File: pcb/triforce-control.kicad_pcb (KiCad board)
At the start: 2 copper layers, 75 x 86 mm, 17 parts, among them CON1 Conn_01x08, CON2 Conn_01x08, CON9 Conn_01x04, U1 ADAFRUIT_HUZZAH, U2 bno055, U3 LPC1768, U4 SN65HVD232

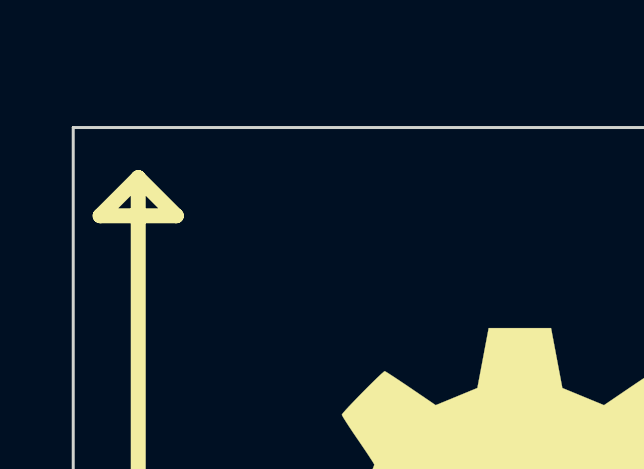
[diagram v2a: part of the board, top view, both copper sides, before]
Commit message: Started adding enclosure parts as footprints.
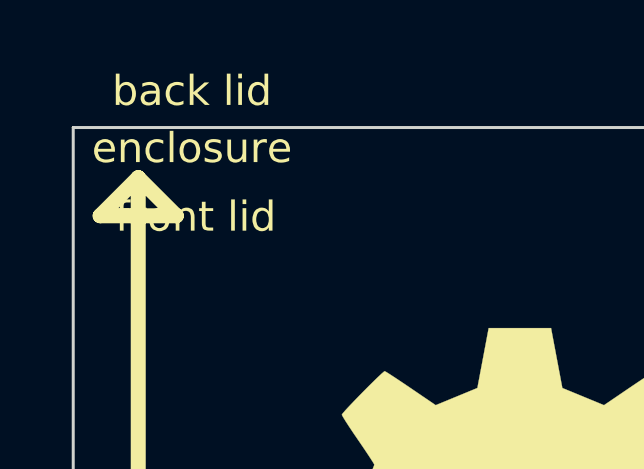
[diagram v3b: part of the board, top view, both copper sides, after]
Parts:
- added back lid: enclosure, Triforce_Fight_Controller:enclosure, F.Cu at (112.1, 51.3)
- added enclosure: enclosure, Triforce_Fight_Controller:enclosure, F.Cu at (112.1, 53.2)
- added enclosure: enclosure, Triforce_Fight_Controller:enclosure, F.Cu at (31.8, 36.7)
- added front lid: enclosure, Triforce_Fight_Controller:enclosure, F.Cu at (112.3, 55.5)
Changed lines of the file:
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@@
 (kicad_pcb (version 4) (host pcbnew 4.0.7-e2-6376~58~ubuntu16.04.1)
   (general
-    (links 52)
+    (links 0)
     (no_connects 0)
     (area 112.068999 53.108999 187.169001 139.209001)
@@
     (tracks 304)
     (zones 0)
-    (modules 17)
+    (modules 21)
     (nets 71)
   )
@@
     (add_net ESP_MBED_RX)
     (add_net ESP_MBED_TX)
+  )
+  (module Triforce_Fight_Controller:enclosure locked (layer F.Cu)
+    (at 112.268 55.499)
+    (attr virtual)
+    (fp_text reference "front lid" (at 3.937 0.635) (layer F.SilkS)
+      (effects (font (size 1 1) (thickness 0.15)))
+    )
+    (fp_text value enclosure (at 0 -0.5) (layer F.Fab)
+      (effects (font (size 1 1) (thickness 0.15)))
+    )
+    (model "TriforceFightController.3dshapes/J Bezel Closed.wrl"
+      (at (xyz 0.8149999999999999 -3.4 0.2))
+      (scale (xyz 1 1 1))
+      (rotate (xyz -90 0 0))
+    )
+  )
+  (module Triforce_Fight_Controller:enclosure locked (layer F.Cu)
+    (at 112.141 51.308)
+    (attr virtual)
+    (fp_text reference "back lid" (at 3.937 0.635) (layer F.SilkS)
+      (effects (font (size 1 1) (thickness 0.15)))
+    )
+    (fp_text value enclosure (at 0 -0.5) (layer F.Fab)
+      (effects (font (size 1 1) (thickness 0.15)))
+    )
+    (model "TriforceFightController.3dshapes/J Bezel Closed.wrl"
+      (at (xyz 0.8149999999999999 1.2 0.2))
+      (scale (xyz 1 1 1))
+      (rotate (xyz -270 0 0))
+    )
   )
   (module Symbols:KiCad-Logo2_6mm_SilkScreen (layer F.Cu)
@@
       (at (xyz 0 0 0))
       (scale (xyz 1 1 1))
+      (rotate (xyz 0 0 0))
+    )
+  )
+  (module Triforce_Fight_Controller:enclosure locked (layer F.Cu)
+    (at 112.141 53.213)
+    (attr virtual)
+    (fp_text reference enclosure (at 3.937 0.635) (layer F.SilkS)
+      (effects (font (size 1 1) (thickness 0.15)))
+    )
+    (fp_text value enclosure (at 0 -0.5) (layer F.Fab)
+      (effects (font (size 1 1) (thickness 0.15)))
+    )
+    (model "TriforceFightController.3dshapes/J Extrusion001.wrl"
+      (at (xyz 1.47 -3.4 0.71))
+      (scale (xyz 1 1 1))
+      (rotate (xyz 90 0 0))
+    )
+    (model "TriforceFightController.3dshapes/J Extrusion.wrl"
+      (at (xyz 1.47 -3.4 0.71))
+      (scale (xyz 1 1 1))
+      (rotate (xyz 90 0 0))
+    )
+  )
+  (module Triforce_Fight_Controller:enclosure (layer F.Cu)
+    (at 31.75 36.703)
+    (fp_text reference enclosure (at 0 1.27) (layer F.SilkS) hide
+      (effects (font (size 1 1) (thickness 0.15)))
+    )
+    (fp_text value enclosure (at 0 -0.5) (layer F.Fab)
+      (effects (font (size 1 1) (thickness 0.15)))
+    )
+    (model "TriforceFightController.3dshapes/J Extrusion001.wrl"
+      (at (xyz 0 0 0))
+      (scale (xyz 1 1 1))
+      (rotate (xyz 0 0 0))
+    )
+    (model "TriforceFightController.3dshapes/J Extrusion.wrl"
+      (at (xyz 0 0 0))
+      (scale (xyz 1 1 1))

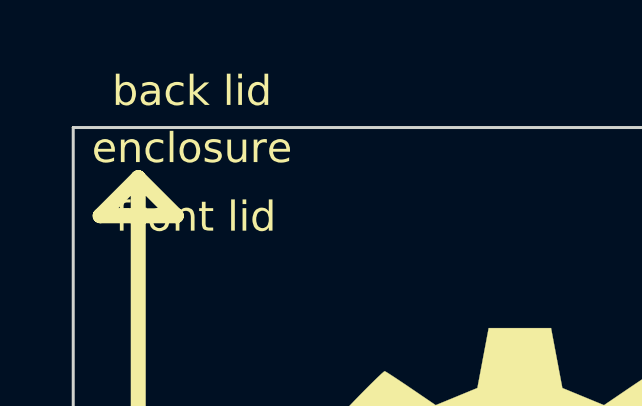
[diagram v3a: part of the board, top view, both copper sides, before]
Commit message: Added enclosure 3d shapes to PCB.
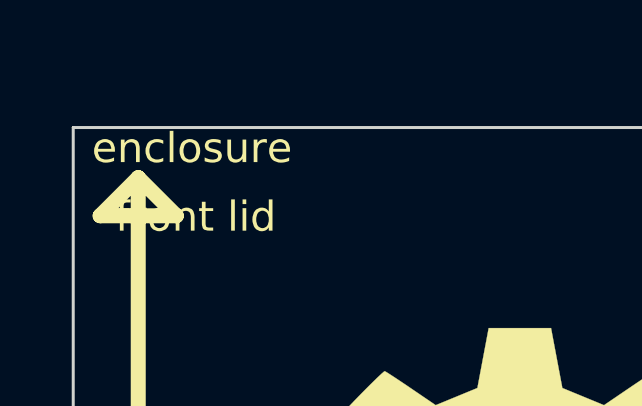
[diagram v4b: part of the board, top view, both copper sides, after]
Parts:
- removed the enclosure at (31.8, 36.7)
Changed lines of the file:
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@@
 (kicad_pcb (version 4) (host pcbnew 4.0.7-e2-6376~58~ubuntu16.04.1)
   (general
-    (links 0)
+    (links 52)
     (no_connects 0)
     (area 112.068999 53.108999 187.169001 139.209001)
@@
     (tracks 304)
     (zones 0)
-    (modules 21)
+    (modules 20)
     (nets 71)
   )
@@
     (at 112.141 51.308)
     (attr virtual)
-    (fp_text reference "back lid" (at 3.937 0.635) (layer F.SilkS)
+    (fp_text reference "back lid" (at 3.937 0.635) (layer F.SilkS) hide
       (effects (font (size 1 1) (thickness 0.15)))
     )
@@
     )
     (model "TriforceFightController.3dshapes/J Bezel Closed.wrl"
-      (at (xyz 0.8149999999999999 1.2 0.2))
+      (at (xyz 0.8149999999999999 1.2 0.3))
       (scale (xyz 1 1 1))
       (rotate (xyz -270 0 0))
@@
     )
   )
-  (module Triforce_Fight_Controller:enclosure (layer F.Cu)
-    (at 31.75 36.703)
-    (fp_text reference enclosure (at 0 1.27) (layer F.SilkS) hide
-      (effects (font (size 1 1) (thickness 0.15)))
-    )
-    (fp_text value enclosure (at 0 -0.5) (layer F.Fab)
-      (effects (font (size 1 1) (thickness 0.15)))
-    )
-    (model "TriforceFightController.3dshapes/J Extrusion001.wrl"
-      (at (xyz 0 0 0))
-      (scale (xyz 1 1 1))
-      (rotate (xyz 0 0 0))
-    )
-    (model "TriforceFightController.3dshapes/J Extrusion.wrl"
-      (at (xyz 0 0 0))
-      (scale (xyz 1 1 1))
-      (rotate (xyz 0 0 0))
-    )
-  )

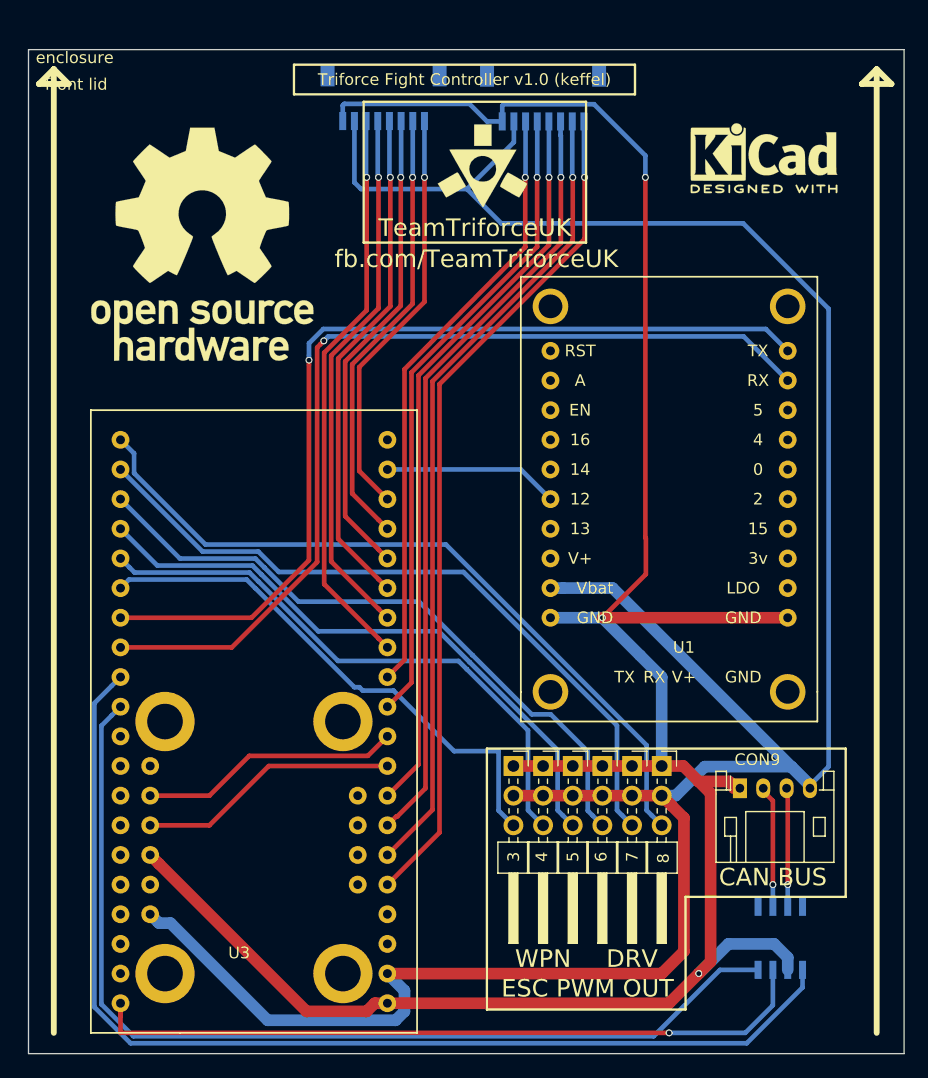
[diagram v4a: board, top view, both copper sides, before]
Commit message: Started v2.x work, integrating developement boards into PCB.
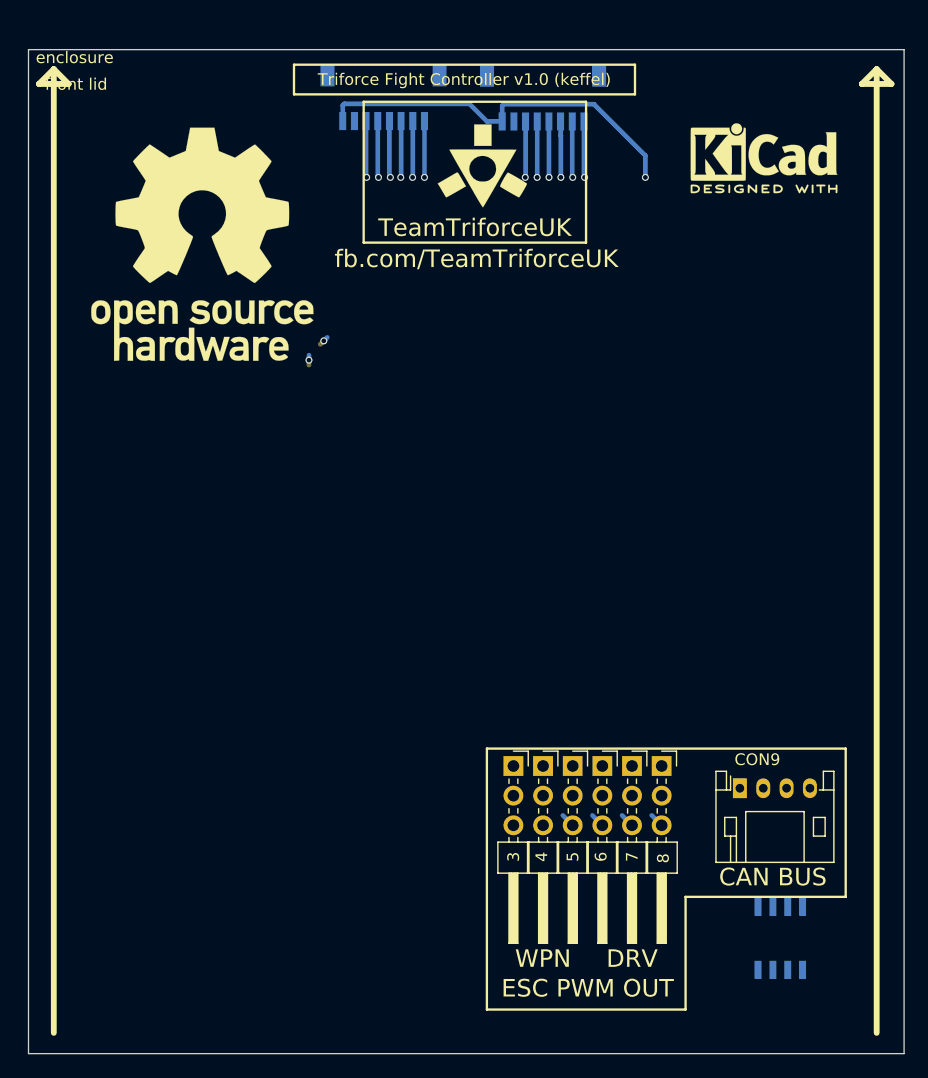
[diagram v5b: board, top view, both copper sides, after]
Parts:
- removed U1: ADAFRUIT_HUZZAH, Triforce_Fight_Controller:ESP8266
- removed U2: bno055, Triforce_Fight_Controller:BNO055
- removed U3: LPC1768, Triforce_Fight_Controller:lpc1768
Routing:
- net +5V: track 225.9 -> 0.25 mm
- net GND: track 208.8 -> 33.3 mm, vias 3 -> 1
- net CAN_TXD: track 94.6 -> 0.00 mm
- net CAN_RXD: track 85.9 -> 0.00 mm
- net ESP_MBED_TX: track 80.5 -> 0.85 mm
- net ESP_MBED_RX: track 79.1 -> 0.85 mm
- net IN_RX_W6: track 72.5 -> 4.82 mm
- net IN_RX_W5: track 69.4 -> 4.81 mm
- net MBED_3V3: track 63.5 -> 0.00 mm, vias 1 -> 0
- net PWM_OUT_DRV_MOTOR_3: track 64.3 -> 1.20 mm
- net IN_RX_W4: track 66.5 -> 4.80 mm
- net PWM_OUT_DRV_MOTOR_2: track 60.7 -> 1.20 mm
- net IN_RX_W3: track 63.5 -> 4.80 mm
- net PWM_OUT_DRV_MOTOR_1: track 55.8 -> 1.20 mm
- net PWM_OUT_WPN_MOTOR_3: track 52.3 -> 1.20 mm
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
